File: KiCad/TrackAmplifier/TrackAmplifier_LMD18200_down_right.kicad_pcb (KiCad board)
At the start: 2 copper layers, 105 x 70 mm, 96 parts, among them J1 DB15_Male_MountingHoles, J2 Conn_01x06, Q1 2N7002, U1 ST485EBDR, U10 REF3025, U11 LM35-LP, U2 ST485EBDR, U3 LM78M05_TO252, U4 LMD18200, U5 ST485EBDR, U6 ST485EBDR, U7 INA326, U8 INA326, U9 PIC16F18854-SO

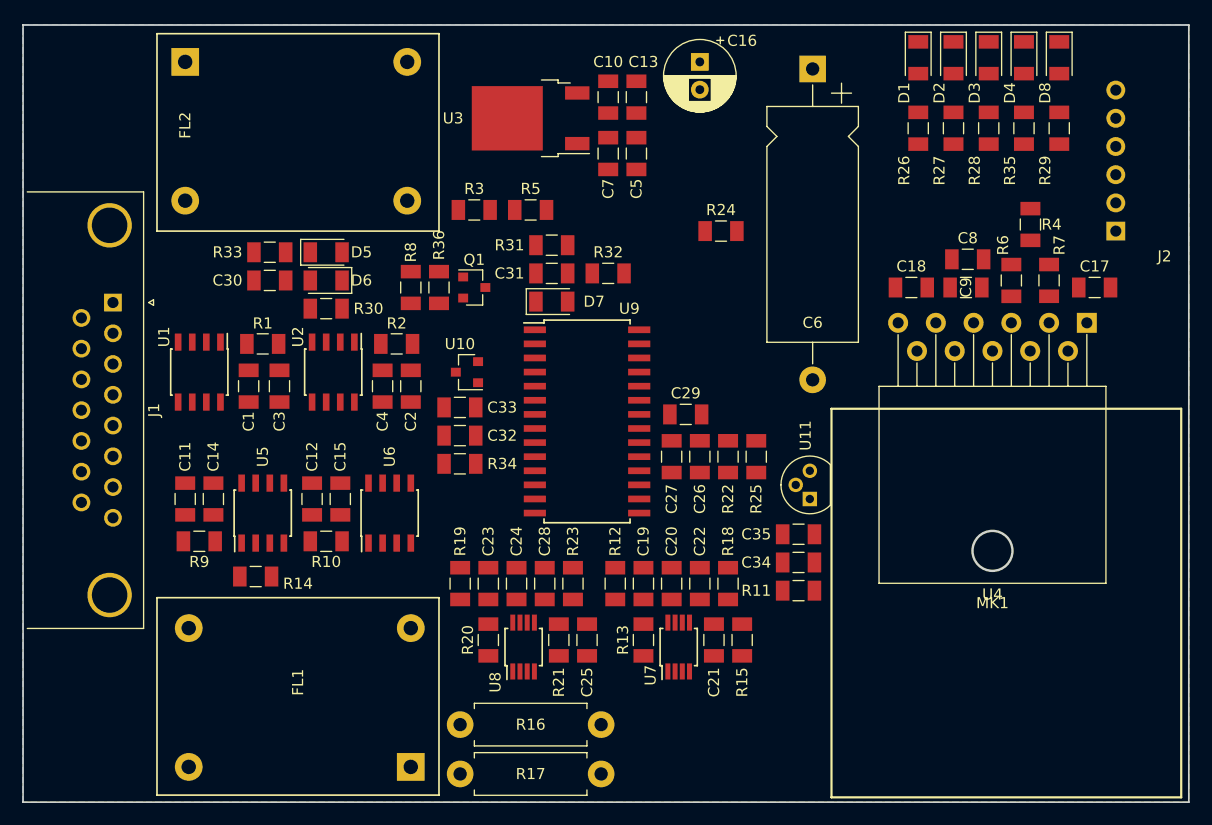
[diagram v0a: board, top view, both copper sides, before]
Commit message: Updated TrackAmplifier.kicad_pcb and created a backup version called TrackAmplifier/TrackAmplifier_LMD18200_down_right.sch and TrackAmplifier/TrackAmplifier_LMD18200_down_right.kicad_pcb were components have a diffeent orientation
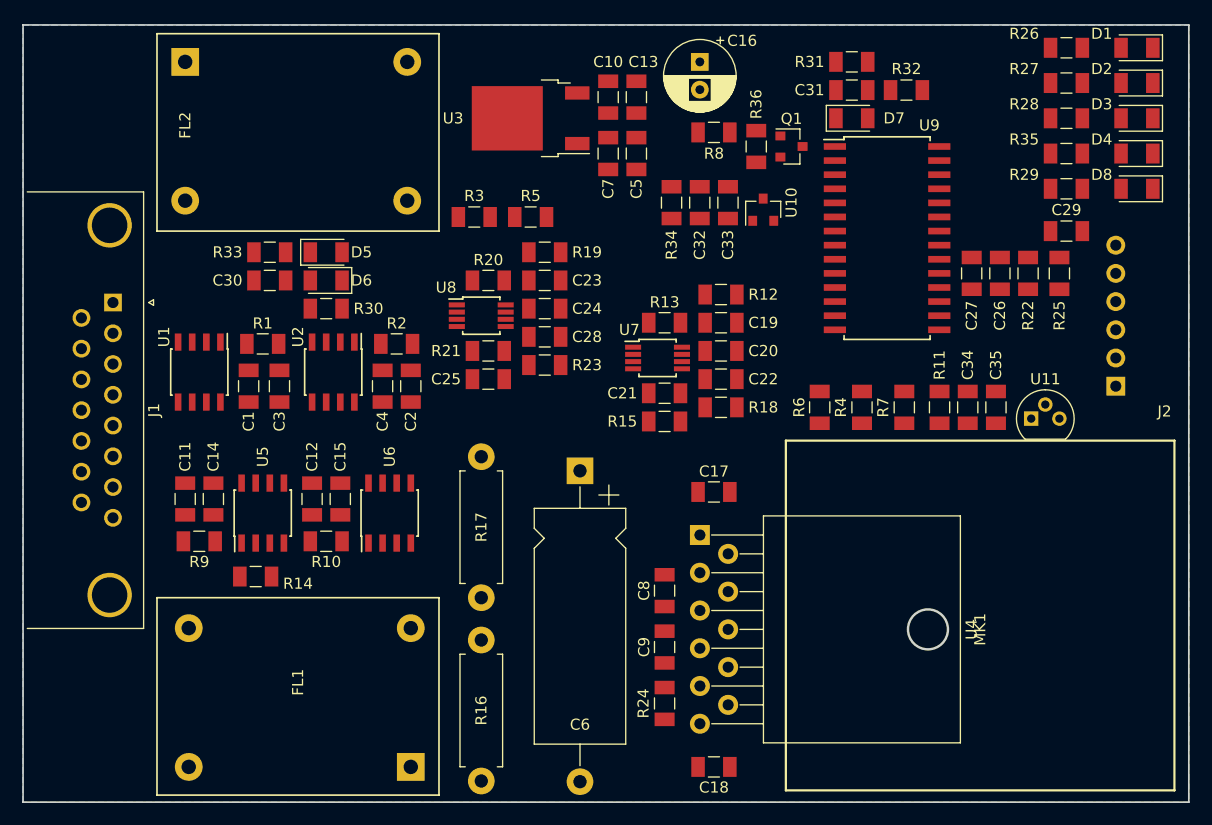
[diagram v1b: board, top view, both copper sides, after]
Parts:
- moved C18 46.7 mm to (112.2, 116.8)
- moved R24 42.8 mm to (107.8, 111.1), turned to 270 degrees
- moved C9 42.3 mm to (107.8, 106.0), turned to 90 degrees
- moved C6 41.8 mm to (100.2, 90.2)
- moved C8 40.5 mm to (107.8, 101.0), turned to 90 degrees
- moved U4 39.7 mm to (111.0, 95.9), turned to 270 degrees
- moved C17 38.9 mm to (112.2, 92.1), turned to 0 degrees
- moved C29 38.1 mm to (144.0, 68.6)
- moved R20 32.4 mm to (91.9, 73.0), turned to 0 degrees
- moved R25 31.9 mm to (143.3, 72.4)
- moved C27 31.7 mm to (135.4, 72.4)
- moved D7 31.7 mm to (124.6, 58.4)
- moved C31 31.7 mm to (124.6, 55.9)
- moved R31 31.7 mm to (124.6, 53.3)
- moved R22 31.7 mm to (140.5, 72.4)
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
